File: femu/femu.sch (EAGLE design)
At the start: 47 parts, among them IC1 ESP32-QFN_5X5, IC3 FT230XQ, U1 LP5900TL-3.0/NOPB

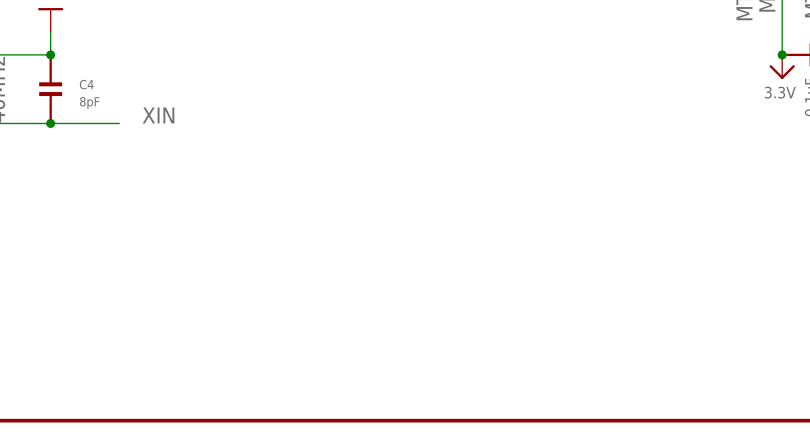
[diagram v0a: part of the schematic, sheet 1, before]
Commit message: Adding fiducials and stencil jig holes, adjusting dimension labels
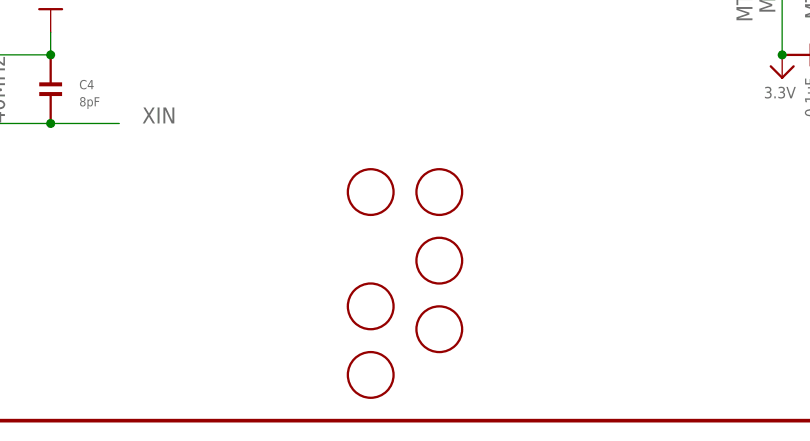
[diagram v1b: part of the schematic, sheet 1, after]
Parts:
- added FID1, FID2, FID3, FID4, FID5, FID6: FIDUCIAL, adafruit:FIDUCIAL
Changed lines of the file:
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@@
 </part>
 <part name="U$20" library="microbuilder" deviceset="VIN" device=""/>
+<part name="FID1" library="adafruit" deviceset="FIDUCIAL" device=""/>
+<part name="FID2" library="adafruit" deviceset="FIDUCIAL" device=""/>
+<part name="FID3" library="adafruit" deviceset="FIDUCIAL" device=""/>
+<part name="FID4" library="adafruit" deviceset="FIDUCIAL" device=""/>
+<part name="FID5" library="adafruit" deviceset="FIDUCIAL" device=""/>
+<part name="FID6" library="adafruit" deviceset="FIDUCIAL" device=""/>
 </parts>
 <sheets>
@@
 <attribute name="VALUE" x="53.34" y="133.096" size="1.27" layer="96" rot="R90"/>
 </instance>
+<instance part="FID1" gate="G$1" x="93.98" y="25.4" smashed="yes"/>
+<instance part="FID2" gate="G$1" x="101.6" y="25.4" smashed="yes"/>
+<instance part="FID3" gate="G$1" x="101.6" y="17.78" smashed="yes"/>
+<instance part="FID4" gate="G$1" x="93.98" y="12.7" smashed="yes"/>
+<instance part="FID5" gate="G$1" x="101.6" y="10.16" smashed="yes"/>
+<instance part="FID6" gate="G$1" x="93.98" y="5.08" smashed="yes"/>
 </instances>
 <busses>

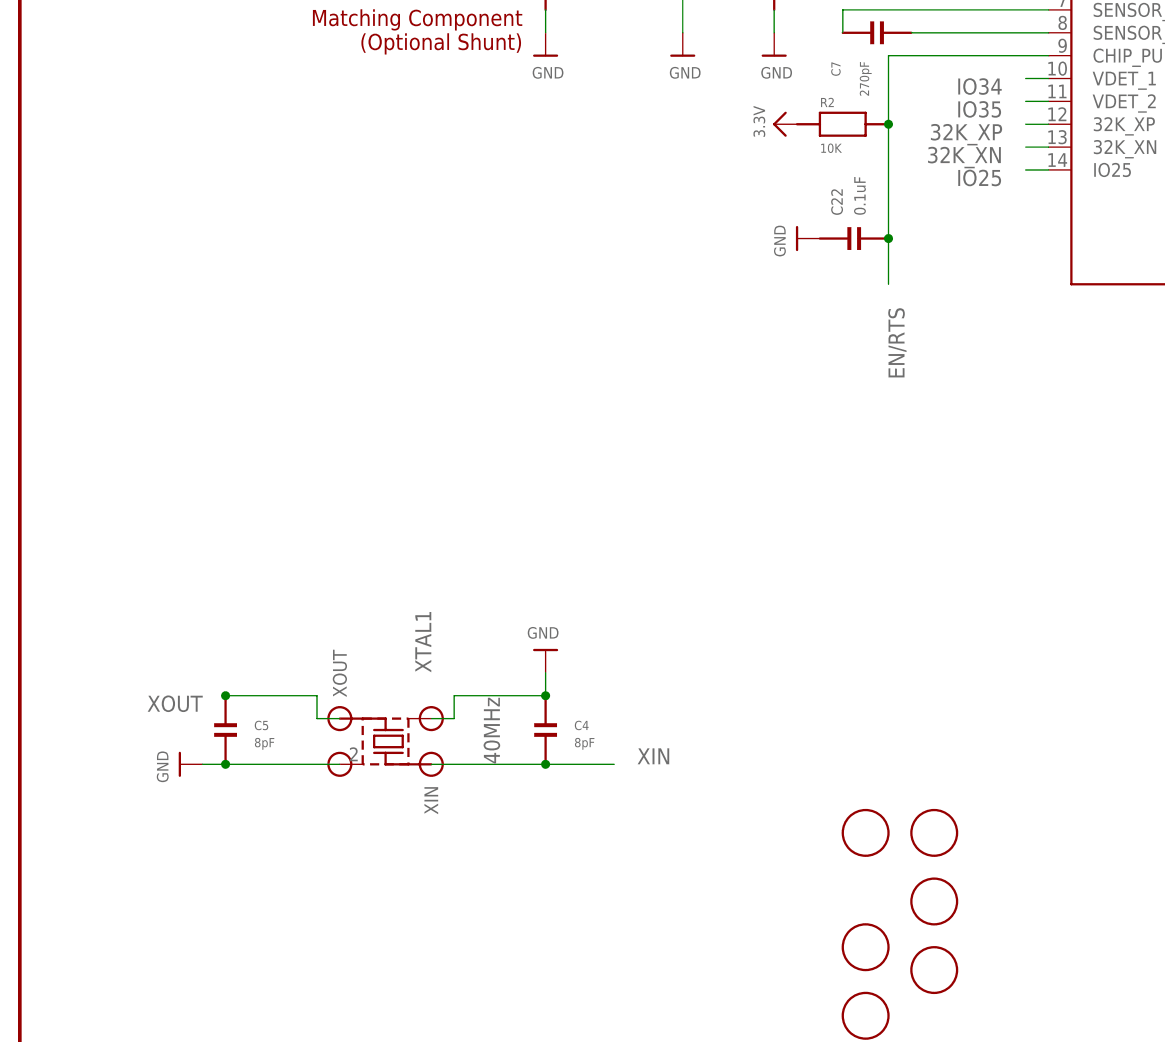
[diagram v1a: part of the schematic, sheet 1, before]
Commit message: Let's try the on semiconductor LDO. Might swap out with something else depending on community guidance regarding heat dissipation. Added edge connectors
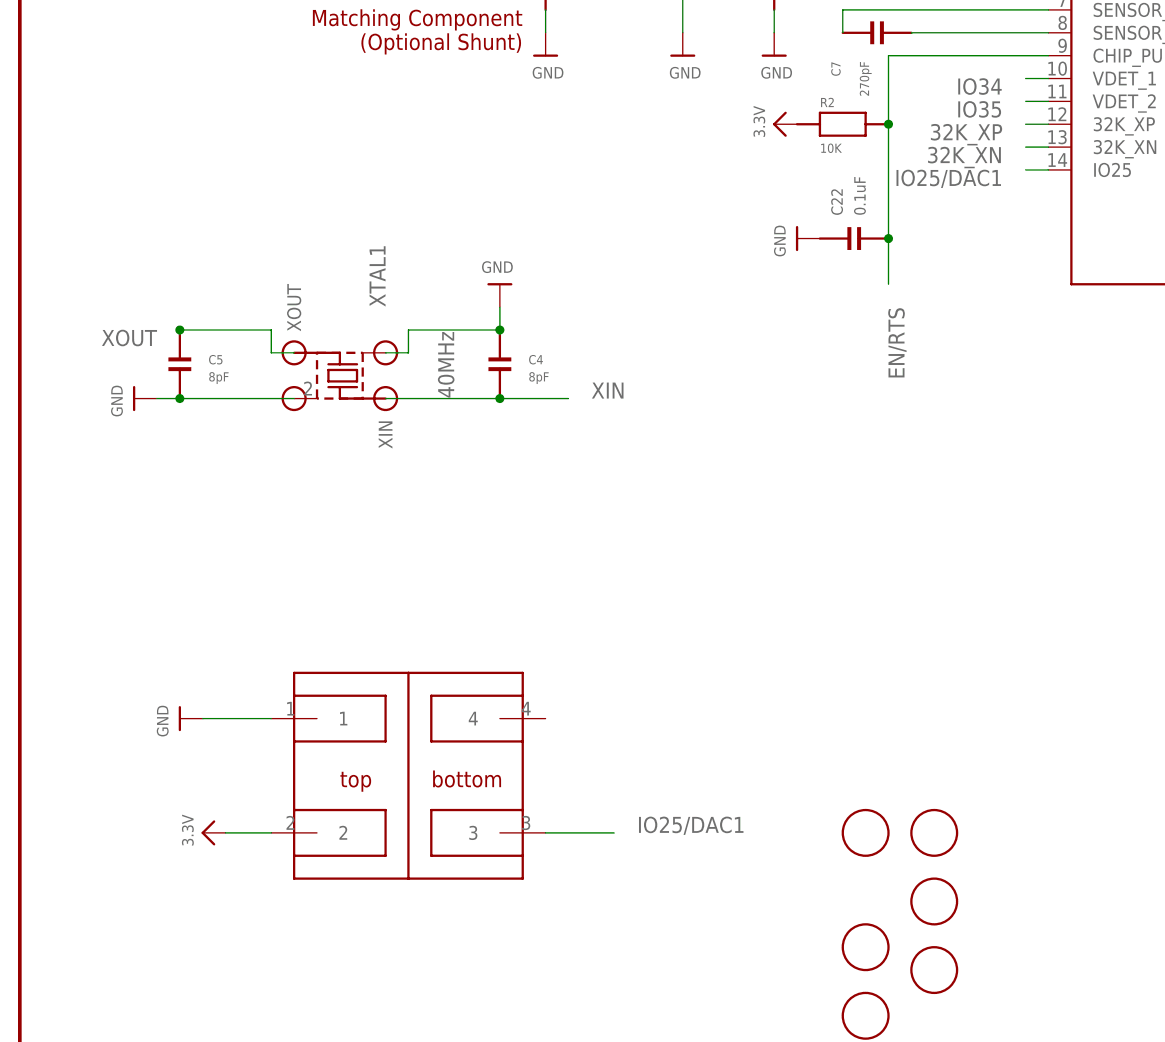
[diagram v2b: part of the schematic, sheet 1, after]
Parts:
- removed U1: LP5900TL-3.0/NOPB, ti-ldo-3.3v-LP5900TL-3.0__NOPB:LP5900TL-3.0/NOPB
- added U$33: NCP167AFCT330T2G, onsemi:NCP167AFCT330T2G
- added U$6: FEMU-EDGE-CONNECTOR, femu-edge-connectors:FEMU-EDGE-CONNECTOR
- C2, C3: value 0.47uF -> 1uF; MPN JMK063BJ474MP-F -> CL03A105KQ3CSNH
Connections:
- removed net IO25: IC1.IO25
- new net IO25/DAC1: IC1.IO25, U$6.3
- net 3.3V: now also C3.P$2, U$33.A2/OUT, U$6.2; no longer C3.P$1, U1.B2/VOUT
- net GND: now also C2.P$1, C3.P$1, U$33.B2/GND, U$6.1; no longer C2.P$2, C3.P$2, U1.B1/GND
- net VIN: now also C2.P$2, U$33.A1/IN, U$33.B1/EN; no longer C2.P$1, U1.A1/VEN, U1.A2/VIN
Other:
- moved on the sheet: C2, C3, C4, C5, XTAL1
